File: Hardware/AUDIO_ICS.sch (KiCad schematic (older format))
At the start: 41 parts, among them U10 PCM1863, U9 PCM9211, X1 24.576 MHz

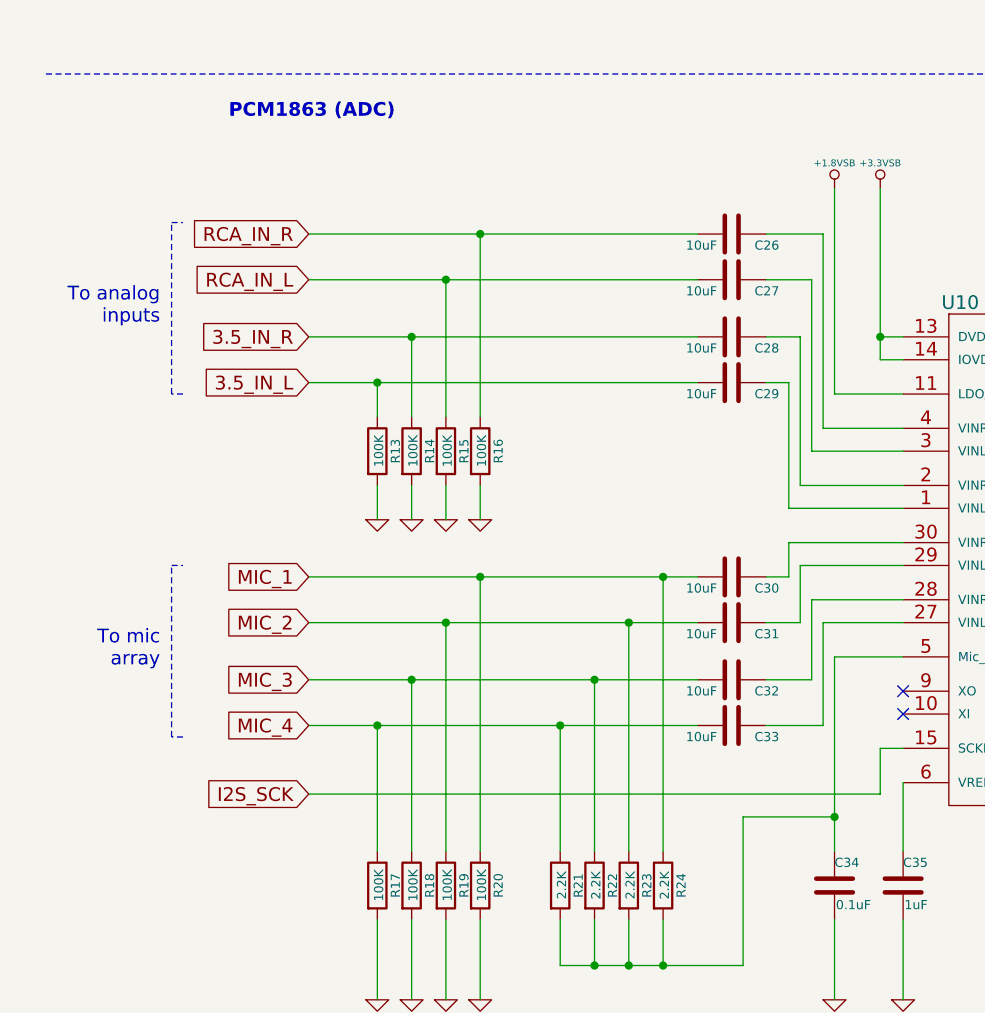
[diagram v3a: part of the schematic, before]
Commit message: All tracks and planes filled.  Fixing fill intersections and missing power/gnd connections
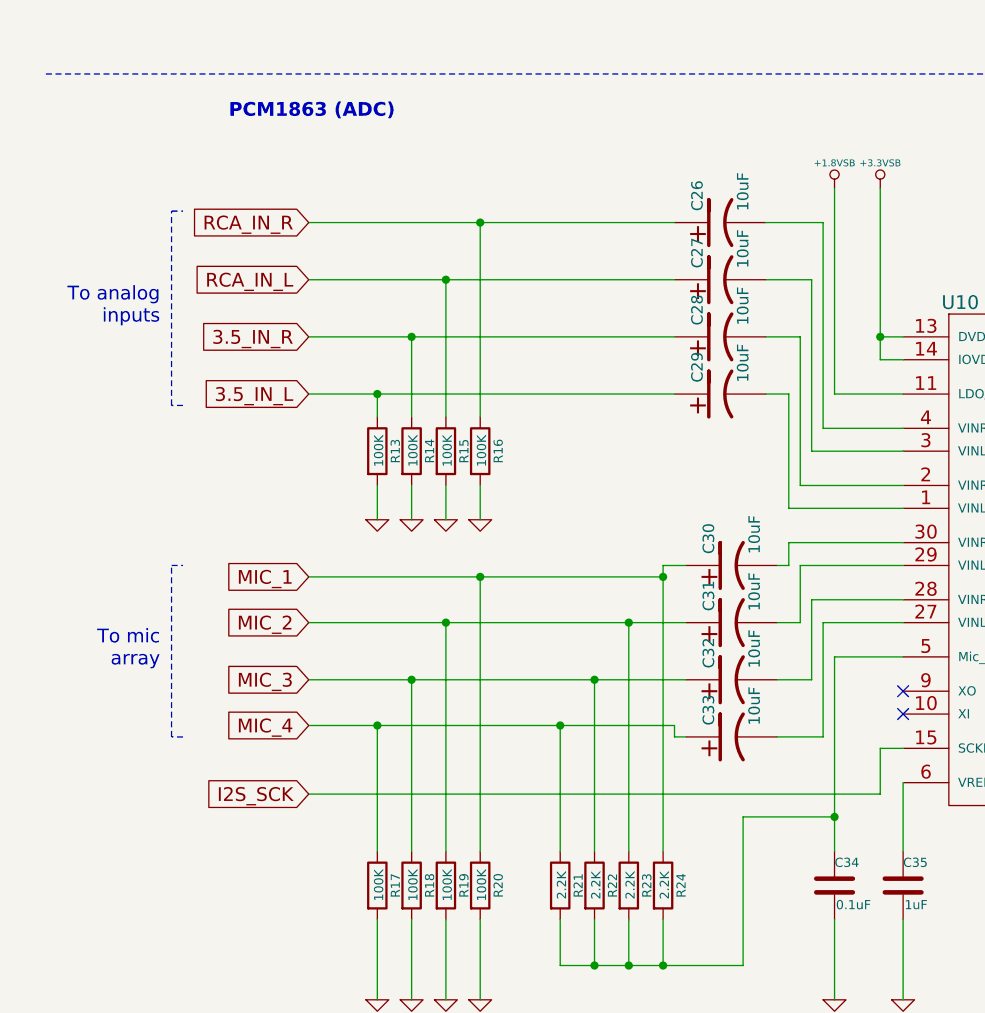
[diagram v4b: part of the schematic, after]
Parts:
- removed C26, C27, C28, C29, C30, C31, C32, C33: 10uF, Capacitors_SMD:c_elec_4x5.3, symbol C-RESCUE-museV2
- added C26, C27, C28, C29, C30, C31, C32, C33: 10uF, symbol CP1
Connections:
- net 3.5_IN_L: now also C29.1
- net 3.5_IN_R: now also C28.1
- net MIC_1: now also C30.1
- net MIC_2: now also C31.1
- net MIC_3: now also C32.1
- net MIC_4: now also C33.1
- net RCA_IN_L: now also C27.1
- net RCA_IN_R: now also C26.1
- net at U10.4 (VINR1/VIN2P): now also C26.2
- net at U10.3 (VINL1/VIN1P): now also C27.2
- net at U10.1 (VINL2/VIN1M): now also C29.2
- net at U10.2 (VINR2/VIN2M): now also C28.2
- net at U10.30 (VINR3/VIN3P): now also C30.2
- net at U10.29 (VINL3/VIN4P): now also C31.2
- net at U10.27 (VINL4/VIN4M): now also C33.2
- net at U10.28 (VINR4/VIN3M): now also C32.2

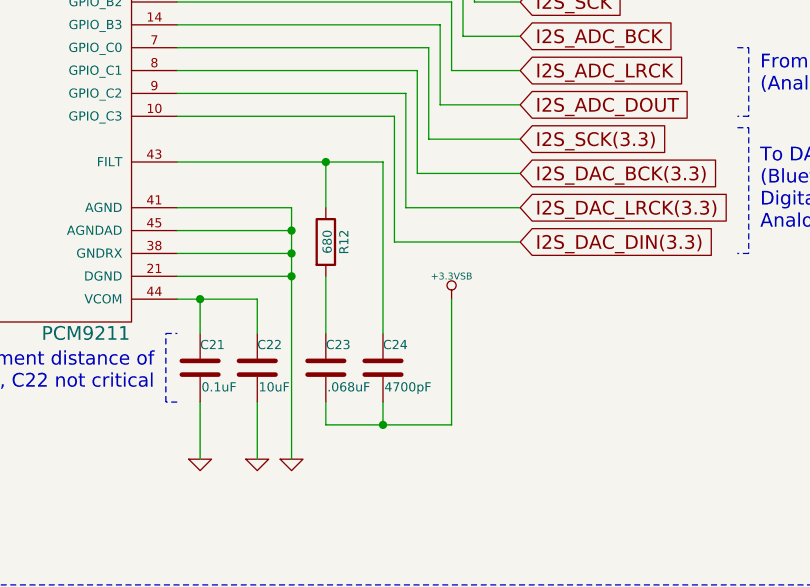
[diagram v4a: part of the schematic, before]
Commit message: Mounting holes added
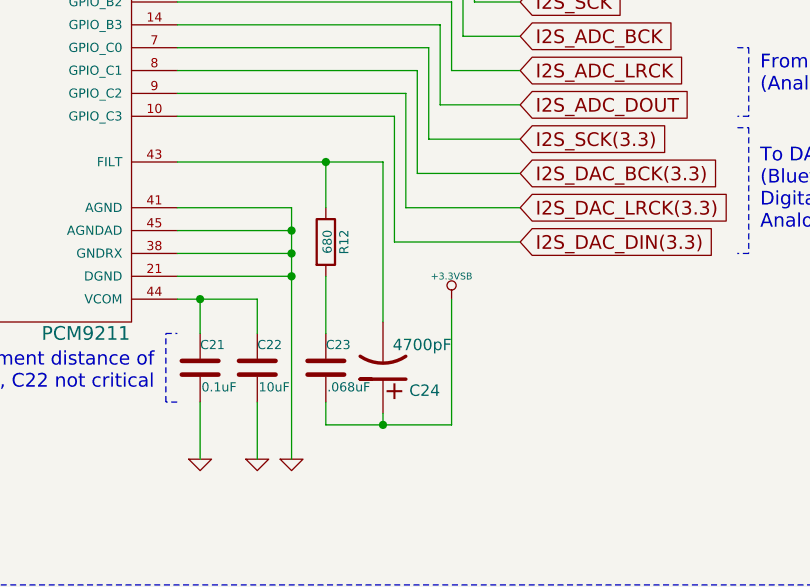
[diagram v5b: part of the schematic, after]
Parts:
- removed C24: 4700pF, Capacitors_SMD:c_elec_4x5.3, symbol C-RESCUE-museV2
- added C24: 4700pF, Capacitors_SMD:C_0805, symbol CP1
- C26, C27, C28, C29, C30, C31, C32, C33: footprint (none) -> Capacitors_SMD:c_elec_4x5.3
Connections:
- net +3.3VSB: now also C24.1
- net at R12.1, U9.43 (FILT): now also C24.2
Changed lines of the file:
@@
-$EndComp
-$Comp
-L C-RESCUE-museV2 C24
-U 1 1 57F2FC70
-P 5700 4700
-F 0 "C24" H 5700 4800 40  0000 L CNN
-F 1 "4700pF" H 5706 4615 40  0000 L CNN
-F 2 "Capacitors_SMD:c_elec_4x5.3" H 5738 4550 30  0001 C CNN
-F 3 "" H 5700 4700 60  0000 C CNN
-	1    5700 4700
-	1    0    0    -1
 $EndComp
 $Comp
@@
 Connection ~ 5450 3800
 Wire Wire Line
-	5700 3800 5700 4550
-Wire Wire Line
 	4800 3800 5700 3800
 Wire Wire Line
@@
 Wire Wire Line
 	5450 4300 5450 4550
-Wire Wire Line
-	5700 4850 5700 4950
 Wire Wire Line
 	5450 4850 5450 4950
@@
 F 0 "C30" H 3550 7900 50  0000 L CNN
 F 1 "10uF" H 3550 7700 50  0000 L CNN
-F 2 "" H 3500 7800 60  0000 C CNN
+F 2 "Capacitors_SMD:c_elec_4x5.3" H 3500 7800 60  0001 C CNN
 F 3 "" H 3500 7800 60  0000 C CNN
 	1    3500 7800
@@
 F 0 "C31" H 3550 8150 50  0000 L CNN
 F 1 "10uF" H 3550 7950 50  0000 L CNN
-F 2 "" H 3500 8050 60  0000 C CNN
+F 2 "Capacitors_SMD:c_elec_4x5.3" H 3500 8050 60  0001 C CNN
 F 3 "" H 3500 8050 60  0000 C CNN
 	1    3500 8050
@@
 F 0 "C32" H 3550 8400 50  0000 L CNN
 F 1 "10uF" H 3550 8200 50  0000 L CNN
-F 2 "" H 3500 8300 60  0000 C CNN
+F 2 "Capacitors_SMD:c_elec_4x5.3" H 3500 8300 60  0001 C CNN
 F 3 "" H 3500 8300 60  0000 C CNN
 	1    3500 8300
@@
 F 0 "C33" H 3550 8650 50  0000 L CNN
 F 1 "10uF" H 3550 8450 50  0000 L CNN
-F 2 "" H 3500 8550 60  0000 C CNN
+F 2 "Capacitors_SMD:c_elec_4x5.3" H 3500 8550 60  0001 C CNN
 F 3 "" H 3500 8550 60  0000 C CNN
 	1    3500 8550
@@
 F 0 "C26" H 3500 6400 50  0000 L CNN
 F 1 "10uF" H 3500 6200 50  0000 L CNN
-F 2 "" H 3450 6300 60  0000 C CNN
+F 2 "Capacitors_SMD:c_elec_4x5.3" H 3450 6300 60  0001 C CNN
 F 3 "" H 3450 6300 60  0000 C CNN
 	1    3450 6300
@@
 F 0 "C27" H 3500 6650 50  0000 L CNN
 F 1 "10uF" H 3500 6450 50  0000 L CNN
-F 2 "" H 3450 6550 60  0000 C CNN
+F 2 "Capacitors_SMD:c_elec_4x5.3" H 3450 6550 60  0001 C CNN
 F 3 "" H 3450 6550 60  0000 C CNN
 	1    3450 6550
@@
 F 0 "C28" H 3500 6900 50  0000 L CNN
 F 1 "10uF" H 3500 6700 50  0000 L CNN
-F 2 "" H 3450 6800 60  0000 C CNN
+F 2 "Capacitors_SMD:c_elec_4x5.3" H 3450 6800 60  0001 C CNN
 F 3 "" H 3450 6800 60  0000 C CNN
 	1    3450 6800
@@
 F 0 "C29" H 3500 7150 50  0000 L CNN
 F 1 "10uF" H 3500 6950 50  0000 L CNN
-F 2 "" H 3450 7050 60  0000 C CNN
+F 2 "Capacitors_SMD:c_elec_4x5.3" H 3450 7050 60  0001 C CNN
 F 3 "" H 3450 7050 60  0000 C CNN
 	1    3450 7050
 	0    -1   -1   0
 $EndComp
+$Comp
+L CP1 C24
+U 1 1 586EBC36
+P 5700 4700
+F 0 "C24" H 5450 4800 50  0000 L CNN
+F 1 "4700pF" H 5400 4600 50  0000 L CNN
+F 2 "Capacitors_SMD:C_0805" H 5700 4700 60  0001 C CNN
+F 3 "" H 5700 4700 60  0000 C CNN
+	1    5700 4700
+	-1   0    0    1
+$EndComp
+Wire Wire Line
+	5700 4950 5700 4900
+Wire Wire Line
+	5700 3800 5700 4500
 $EndSCHEMATC
